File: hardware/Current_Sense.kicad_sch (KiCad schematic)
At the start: 0 parts

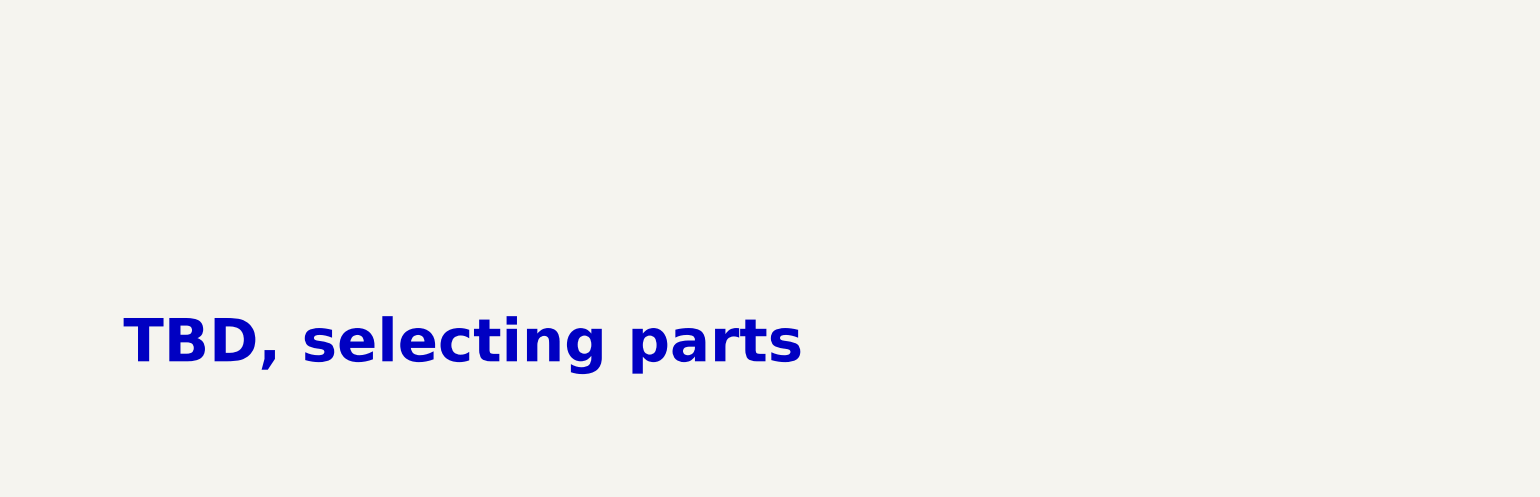
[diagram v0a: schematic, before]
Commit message: added designs for LZSR-80P and AMC class voltage sense
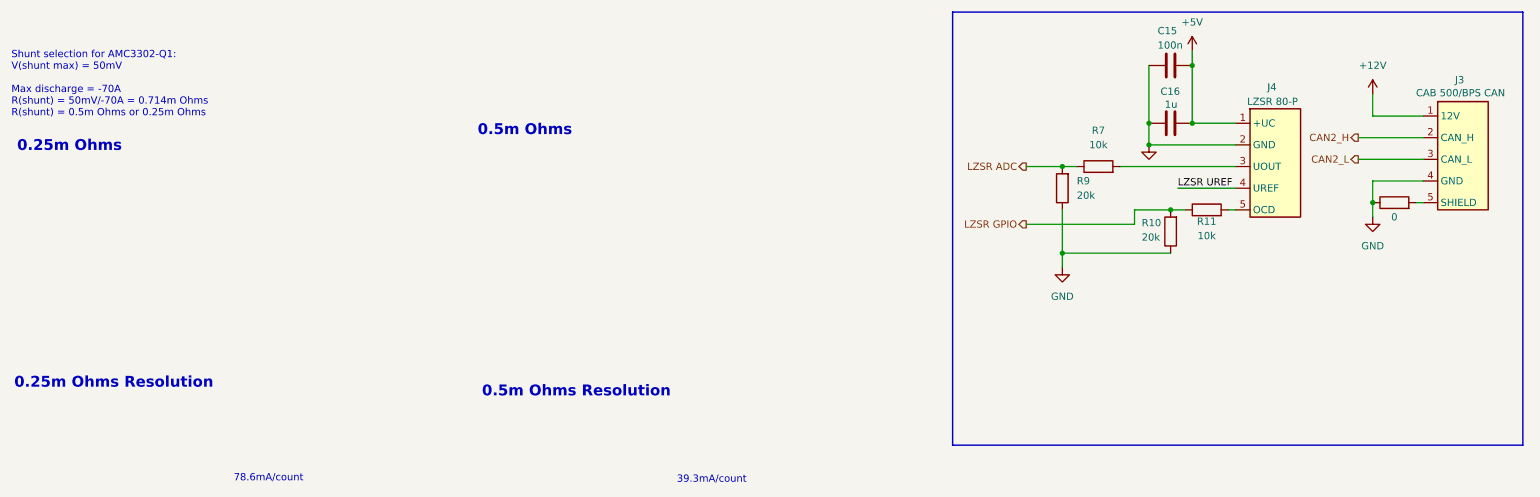
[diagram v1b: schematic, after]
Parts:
- added C15: 100n, symbol Device:C
- added C16: 1u, symbol Device:C
- added J3: CAB 500/BPS CAN, LHRS_Connectors:Molex_Nano-Fit_105309-xx05_1x05_P2.50mm_Vertical, symbol lhrs_connectors:CAN_NANO_01x05
- added J4: LZSR 80-P, LHRS_Connectors:Molex_Nano-Fit_105309-xx05_1x05_P2.50mm_Vertical, symbol lhrs_connectors:CAN_NANO_01x05
- added R10, R9: 20k, symbol Device:R
- added R11, R7: 10k, symbol Device:R
- added R6: 0, symbol Device:R
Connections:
- new net: J3.5 (SHIELD), R6.2
- new net: J4.3 (UOUT), R7.2
- new net: J4.5 (OCD), R11.2
- new net +12V: J3.1 (12V)
- new net +5V: C15.1, C16.1, J4.1 (+UC)
- new net CAN2_H: J3.2 (CAN_H)
- new net CAN2_L: J3.3 (CAN_L)
- new net GND: C15.2, C16.2, J3.4 (GND), J4.2 (GND), R10.1, R6.1, R9.1
- new net LZSR ADC: R7.1, R9.2
- new net LZSR GPIO: R10.2, R11.1
- new net LZSR UREF: J4.4 (UREF)
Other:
- note added: "0.25m Ohms"
- note added: "0.25m Ohms Resolution"
- note added: "0.5m Ohms"
- note added: "0.5m Ohms Resolution"
- note added: "39.3mA/count"
- note added: "78.6mA/count"
- note added: "Shunt selection for AMC3302-Q1: V(shunt max) = 50mV Max discharge = -70A R(shunt) = 50mV/-70A = 0.714m Ohms R(shunt) = 0.5m Ohms or 0.25m Ohms"
- note removed: "TBD, selecting parts"

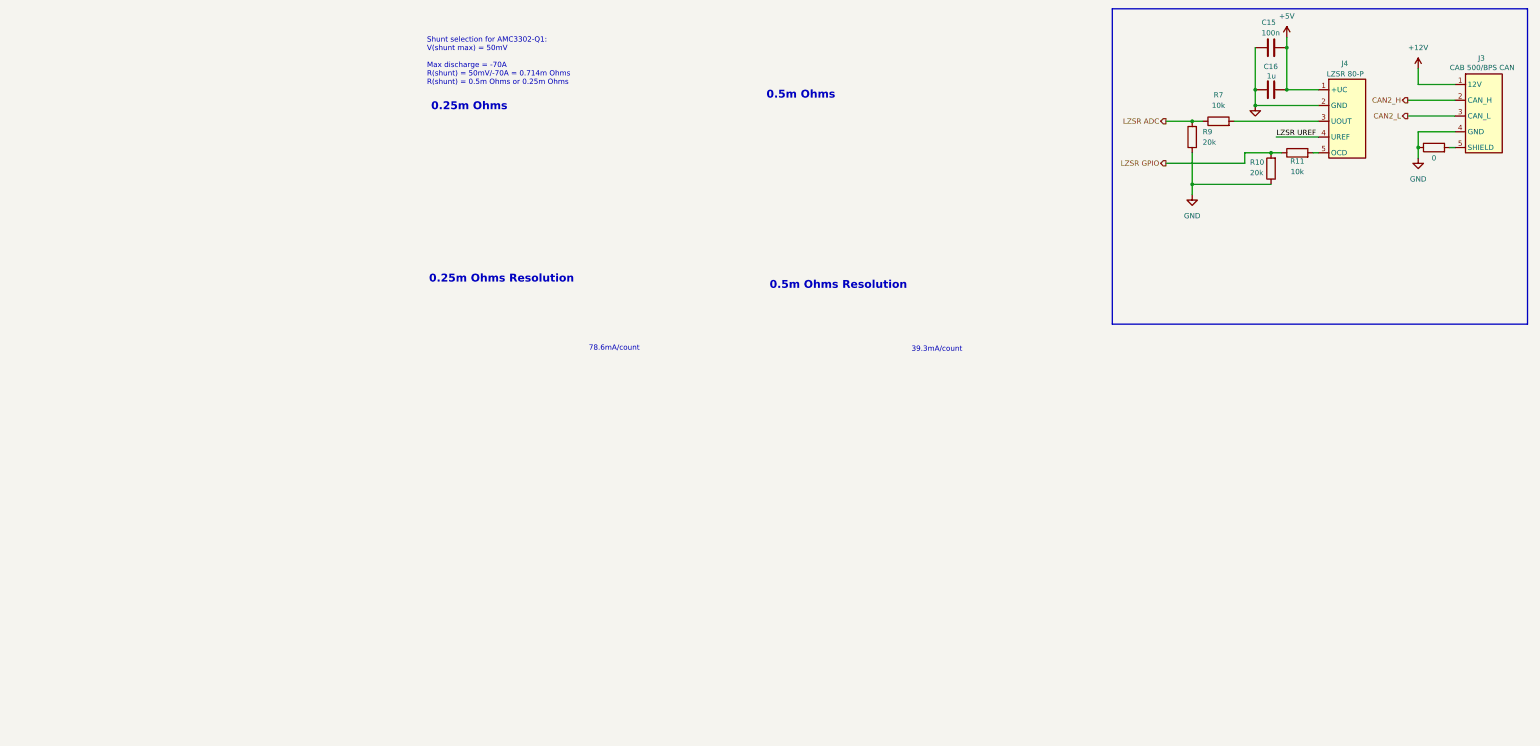
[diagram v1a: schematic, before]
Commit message: labeled + stm32 cube layout
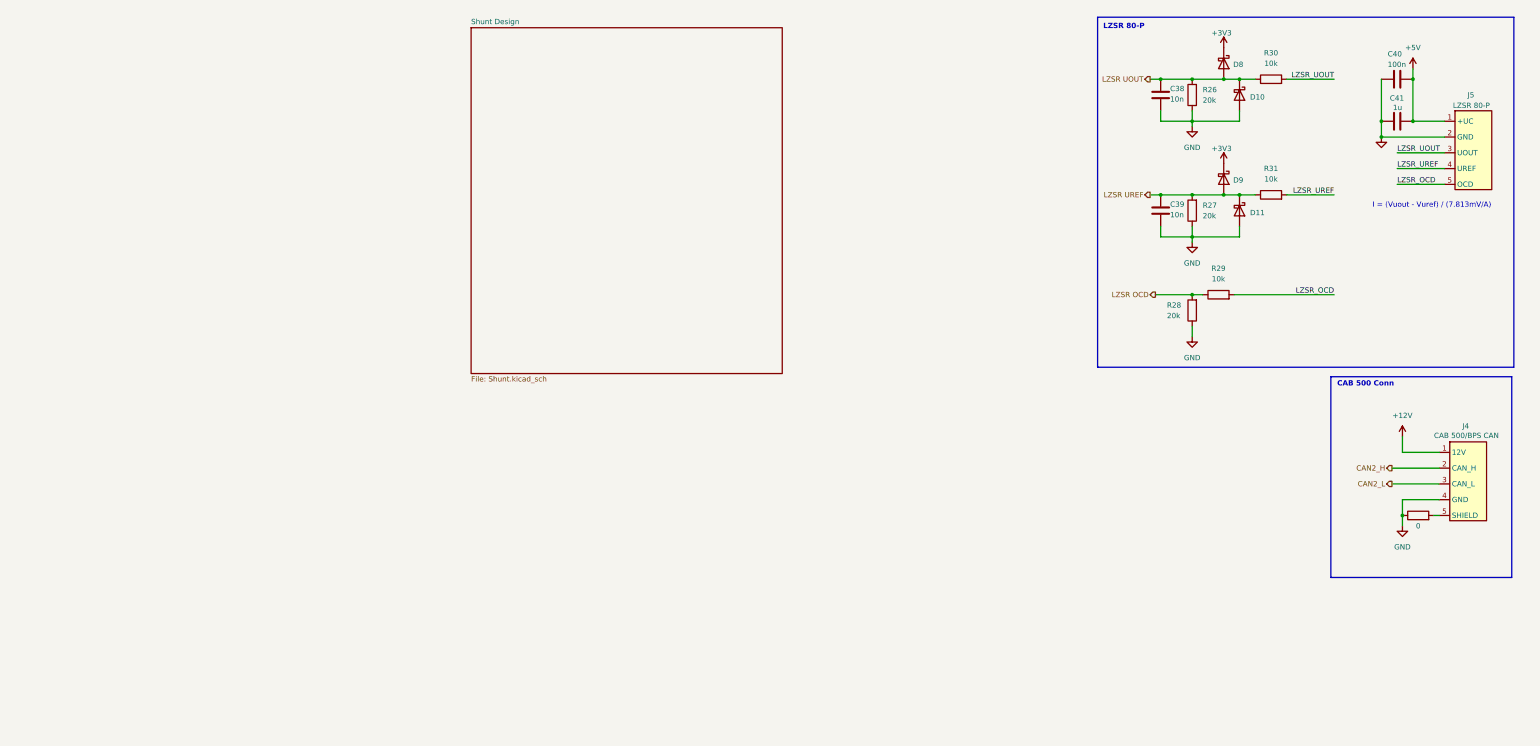
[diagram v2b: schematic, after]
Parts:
- added C38, C39: 10n, symbol Device:C
- added D10, D11, D8, D9: ~, symbol Device:D_Schottky
- added R27: 20k, symbol Device:R
- added R31: 10k, symbol Device:R
- renumbered C15 to C40, C16 to C41, J3 to J4, J4 to J5, R9 to R26, R10 to R28, R11 to R29, R7 to R30, R6 to R32
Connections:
- net GND: now also C38.2, C39.2, D10.2 (A), D11.2 (A), R27.1
- net LZSR UREF: now also C39.1, D11.1 (K), D9.2 (A), R27.2, R31.1; no longer J5.4 (UREF)
- net LZSR_UOUT: now reaches J5.3 (UOUT), R30.2
- net LZSR_OCD: now reaches J5.5 (OCD), R29.2
- net LZSR ADC renamed LZSR UOUT
- net LZSR UOUT: now also C38.1, D10.1 (K), D8.2 (A)
- net LZSR GPIO renamed LZSR OCD
- new net +3V3: D8.1 (K), D9.1 (K)
- new net LZSR_UREF: J5.4 (UREF), R31.2
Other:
- added sheet Shunt Design (Shunt.kicad_sch)
- note added: "CAB 500 Conn"
- note added: "I = (Vuout - Vuref) / (7.813mV/A)"
- note added: "LZSR 80-P"
- note removed: "0.25m Ohms"
- note removed: "0.25m Ohms Resolution"
- note removed: "0.5m Ohms"
- note removed: "0.5m Ohms Resolution"
- note removed: "39.3mA/count"
- note removed: "78.6mA/count"
- note removed: "Shunt selection for AMC3302-Q1: V(shunt max) = 50mV Max discharge = -70A R(shunt) = 50mV/-70A = 0.714m Ohms R(shunt) = 0.5m Ohms or 0.25m Ohms"
- moved on the sheet: C40, C41, J4, J5, R26, R28, R29, R30

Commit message: added debug led
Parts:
- renumbered D8 to D15, D9 to D16, D10 to D17, D11 to D18, R26 to R33, R27 to R34, R28 to R35, R29 to R36, R30 to R37, R31 to R38, R32 to R39
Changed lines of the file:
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@@
 		(dnp no)
 		(fields_autoplaced yes)
-		(property "Reference" "R31"
+		(property "Reference" "R38"
 			(at 222.25 53.34 90)
 			(effects
@@
 			(project "PS-HVCarrier"
 				(path "/2365a867-6254-4a7c-9718-f325e0bbac5c/c64f1e33-0c51-411c-bbbf-0af7b620c655"
-					(reference "R31")
+					(reference "R38")
 					(unit 1)
 				)
@@
 		(dnp no)
 		(fields_autoplaced yes)
-		(property "Reference" "R27"
+		(property "Reference" "R34"
 			(at 205.74 62.2299 0)
 			(effects
@@
 			(project "PS-HVCarrier"
 				(path "/2365a867-6254-4a7c-9718-f325e0bbac5c/c64f1e33-0c51-411c-bbbf-0af7b620c655"
-					(reference "R27")
+					(reference "R34")
 					(unit 1)
 				)
@@
 		(dnp no)
 		(fields_autoplaced yes)
-		(property "Reference" "#PWR043"
+		(property "Reference" "#PWR051"
 			(at 203.2 49.53 0)
 			(effects
@@
 			(project "PS-HVCarrier"
 				(path "/2365a867-6254-4a7c-9718-f325e0bbac5c/c64f1e33-0c51-411c-bbbf-0af7b620c655"
-					(reference "#PWR043")
+					(reference "#PWR051")
 					(unit 1)
 				)
@@
 		(dnp no)
 		(fields_autoplaced yes)
-		(property "Reference" "#PWR051"
+		(property "Reference" "#PWR059"
 			(at 256.54 33.02 0)
 			(effects
@@
 			(project "PS-HVCarrier"
 				(path "/2365a867-6254-4a7c-9718-f325e0bbac5c/c64f1e33-0c51-411c-bbbf-0af7b620c655"
-					(reference "#PWR051")
+					(reference "#PWR059")
 					(unit 1)
 				)
@@
 		(dnp no)
 		(fields_autoplaced yes)
-		(property "Reference" "#PWR044"
+		(property "Reference" "#PWR052"
 			(at 203.2 77.47 0)
 			(effects
@@
 			(project "PS-HVCarrier"
 				(path "/2365a867-6254-4a7c-9718-f325e0bbac5c/c64f1e33-0c51-411c-bbbf-0af7b620c655"
-					(reference "#PWR044")
+					(reference "#PWR052")
 					(unit 1)
 				)
@@
 		(on_board yes)
 		(dnp no)
-		(property "Reference" "#PWR046"
+		(property "Reference" "#PWR054"
 			(at 210.82 27.94 0)
 			(effects
@@
 			(project ""
 				(path "/2365a867-6254-4a7c-9718-f325e0bbac5c/c64f1e33-0c51-411c-bbbf-0af7b620c655"
-					(reference "#PWR046")
+					(reference "#PWR054")
 					(unit 1)
 				)
@@
 		(dnp no)
 		(fields_autoplaced yes)
-		(property "Reference" "R26"
+		(property "Reference" "R33"
 			(at 205.74 34.2899 0)
 			(effects
@@
 			(project "PS-HVCarrier"
 				(path "/2365a867-6254-4a7c-9718-f325e0bbac5c/c64f1e33-0c51-411c-bbbf-0af7b620c655"
-					(reference "R26")
+					(reference "R33")
 					(unit 1)
 				)
@@
 		(on_board yes)
 		(dnp no)
-		(property "Reference" "R28"
+		(property "Reference" "R35"
 			(at 197.104 86.36 0)
 			(effects
@@
 			(project "PS-HVCarrier"
 				(path "/2365a867-6254-4a7c-9718-f325e0bbac5c/c64f1e33-0c51-411c-bbbf-0af7b620c655"
-					(reference "R28")
+					(reference "R35")
 					(unit 1)
 				)
@@
 		(on_board yes)
 		(dnp no)
-		(property "Reference" "D11"
+		(property "Reference" "D18"
 			(at 217.17 64.008 90)
 			(effects
@@
 			(project "PS-HVCarrier"
 				(path "/2365a867-6254-4a7c-9718-f325e0bbac5c/c64f1e33-0c51-411c-bbbf-0af7b620c655"
-					(reference "D11")
+					(reference "D18")
 					(unit 1)
 				)
@@
 		(dnp no)
 		(fields_autoplaced yes)
-		(property "Reference" "#PWR048"
+		(property "Reference" "#PWR056"
 			(at 248.92 52.07 0)
 			(effects
@@
 			(project "PS-HVCarrier"
 				(path "/2365a867-6254-4a7c-9718-f325e0bbac5c/c64f1e33-0c51-411c-bbbf-0af7b620c655"
-					(reference "#PWR048")
+					(reference "#PWR056")
 					(unit 1)
 				)
@@
 		(on_board yes)
 		(dnp no)
-		(property "Reference" "D10"
+		(property "Reference" "D17"
 			(at 217.17 36.068 90)
 			(effects
@@
 			(project "PS-HVCarrier"
 				(path "/2365a867-6254-4a7c-9718-f325e0bbac5c/c64f1e33-0c51-411c-bbbf-0af7b620c655"
-					(reference "D10")
+					(reference "D17")
 					(unit 1)
 				)
@@
 		(on_board yes)
 		(dnp no)
-		(property "Reference" "D9"
+		(property "Reference" "D16"
 			(at 213.106 56.134 90)
 			(effects
@@
 			(project "PS-HVCarrier"
 				(path "/2365a867-6254-4a7c-9718-f325e0bbac5c/c64f1e33-0c51-411c-bbbf-0af7b620c655"
-					(reference "D9")
+					(reference "D16")
 					(unit 1)
 				)
@@
 		(dnp no)
 		(fields_autoplaced yes)
-		(property "Reference" "#PWR050"
+		(property "Reference" "#PWR058"
 			(at 254 146.05 0)
 			(effects
@@
 			(project "PS-HVCarrier"
 				(path "/2365a867-6254-4a7c-9718-f325e0bbac5c/c64f1e33-0c51-411c-bbbf-0af7b620c655"
-					(reference "#PWR050")
+					(reference "#PWR058")
 					(unit 1)
 				)
@@
 		(on_board yes)
 		(dnp no)
-		(property "Reference" "#PWR047"
+		(property "Reference" "#PWR055"
 			(at 210.82 55.88 0)
 			(effects
@@
 			(project "PS-HVCarrier"
 				(path "/2365a867-6254-4a7c-9718-f325e0bbac5c/c64f1e33-0c51-411c-bbbf-0af7b620c655"
-					(reference "#PWR047")
+					(reference "#PWR055")
 					(unit 1)
 				)
@@
 		(dnp no)
 		(fields_autoplaced yes)
-		(property "Reference" "#PWR045"
+		(property "Reference" "#PWR053"
 			(at 203.2 100.33 0)
 			(effects
@@
 			(project ""
 				(path "/2365a867-6254-4a7c-9718-f325e0bbac5c/c64f1e33-0c51-411c-bbbf-0af7b620c655"
-					(reference "#PWR045")
+					(reference "#PWR053")
 					(unit 1)
 				)
@@
 		(on_board yes)
 		(dnp no)
-		(property "Reference" "D8"
+		(property "Reference" "D15"
 			(at 213.106 28.194 90)
 			(effects
@@
 			(project ""
 				(path "/2365a867-6254-4a7c-9718-f325e0bbac5c/c64f1e33-0c51-411c-bbbf-0af7b620c655"
-					(reference "D8")
+					(reference "D15")
 					(unit 1)
 				)
@@
 		(on_board yes)
 		(dnp no)
-		(property "Reference" "R29"
+		(property "Reference" "R36"
 			(at 209.55 77.47 90)
 			(effects
@@
 			(project "PS-HVCarrier"
 				(path "/2365a867-6254-4a7c-9718-f325e0bbac5c/c64f1e33-0c51-411c-bbbf-0af7b620c655"
-					(reference "R29")
+					(reference "R36")
 					(unit 1)
 				)
@@
 		(dnp no)
 		(fields_autoplaced yes)
-		(property "Reference" "#PWR049"
+		(property "Reference" "#PWR057"
 			(at 254 121.92 0)
 			(effects
@@
 			(project "PS-HVCarrier"
 				(path "/2365a867-6254-4a7c-9718-f325e0bbac5c/c64f1e33-0c51-411c-bbbf-0af7b620c655"
-					(reference "#PWR049")
+					(reference "#PWR057")
 					(unit 1)
 				)
@@
 		(on_board yes)
 		(dnp no)
-		(property "Reference" "R32"
+		(property "Reference" "R39"
 			(at 257.81 130.81 90)
 			(effects
@@
 			(project "PS-HVCarrier"
 				(path "/2365a867-6254-4a7c-9718-f325e0bbac5c/c64f1e33-0c51-411c-bbbf-0af7b620c655"
-					(reference "R32")
+					(reference "R39")
 					(unit 1)
 				)
@@
 		(dnp no)
 		(fields_autoplaced yes)
-		(property "Reference" "R30"
+		(property "Reference" "R37"
 			(at 222.25 25.4 90)
 			(effects
@@
 			(project "PS-HVCarrier"
 				(path "/2365a867-6254-4a7c-9718-f325e0bbac5c/c64f1e33-0c51-411c-bbbf-0af7b620c655"
-					(reference "R30")
-					(unit 1)
-				)
+					(reference "R37")
+					(unit 1)
+				)

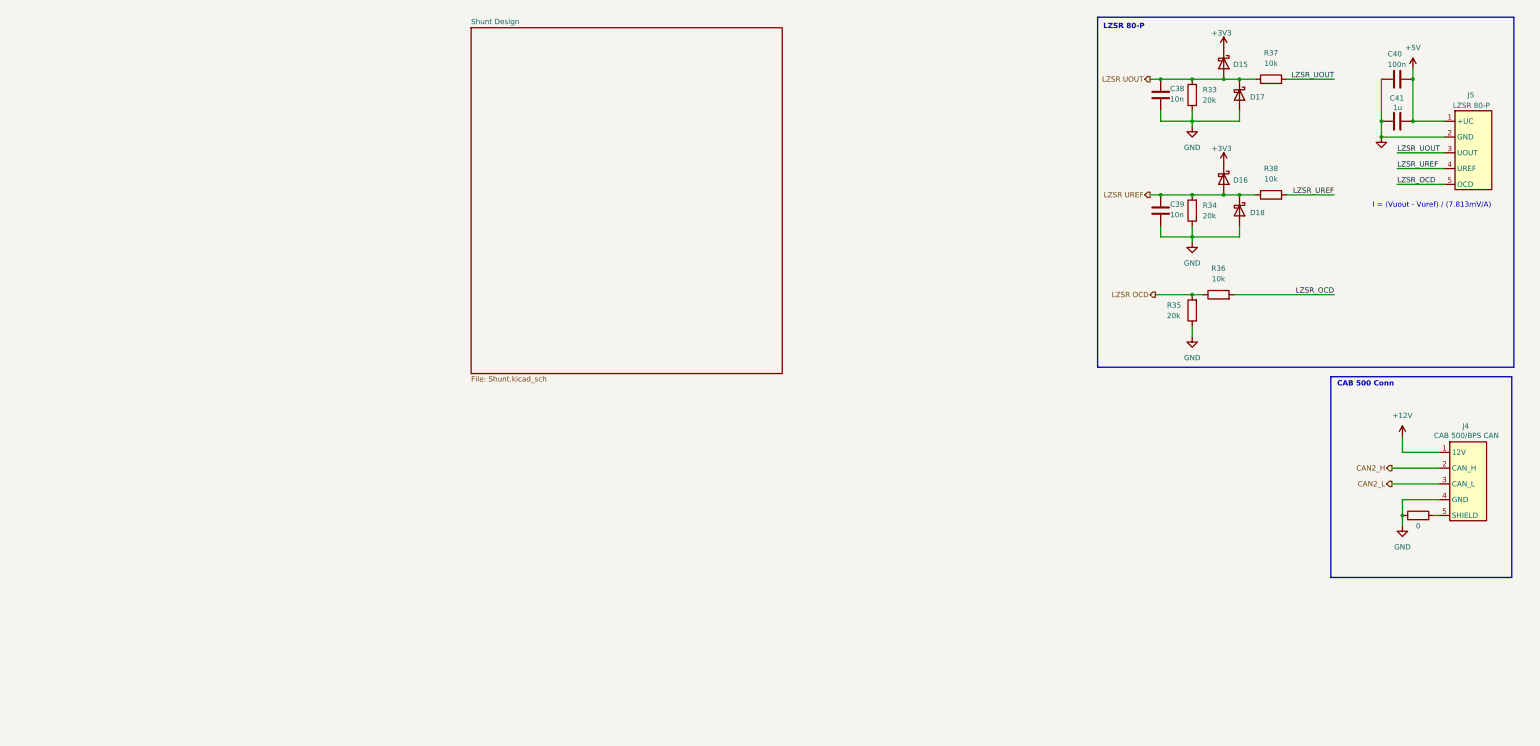
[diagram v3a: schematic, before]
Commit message: addressed 75% of review council 2, cleaned up ERC errors, embedded datasheet and PN
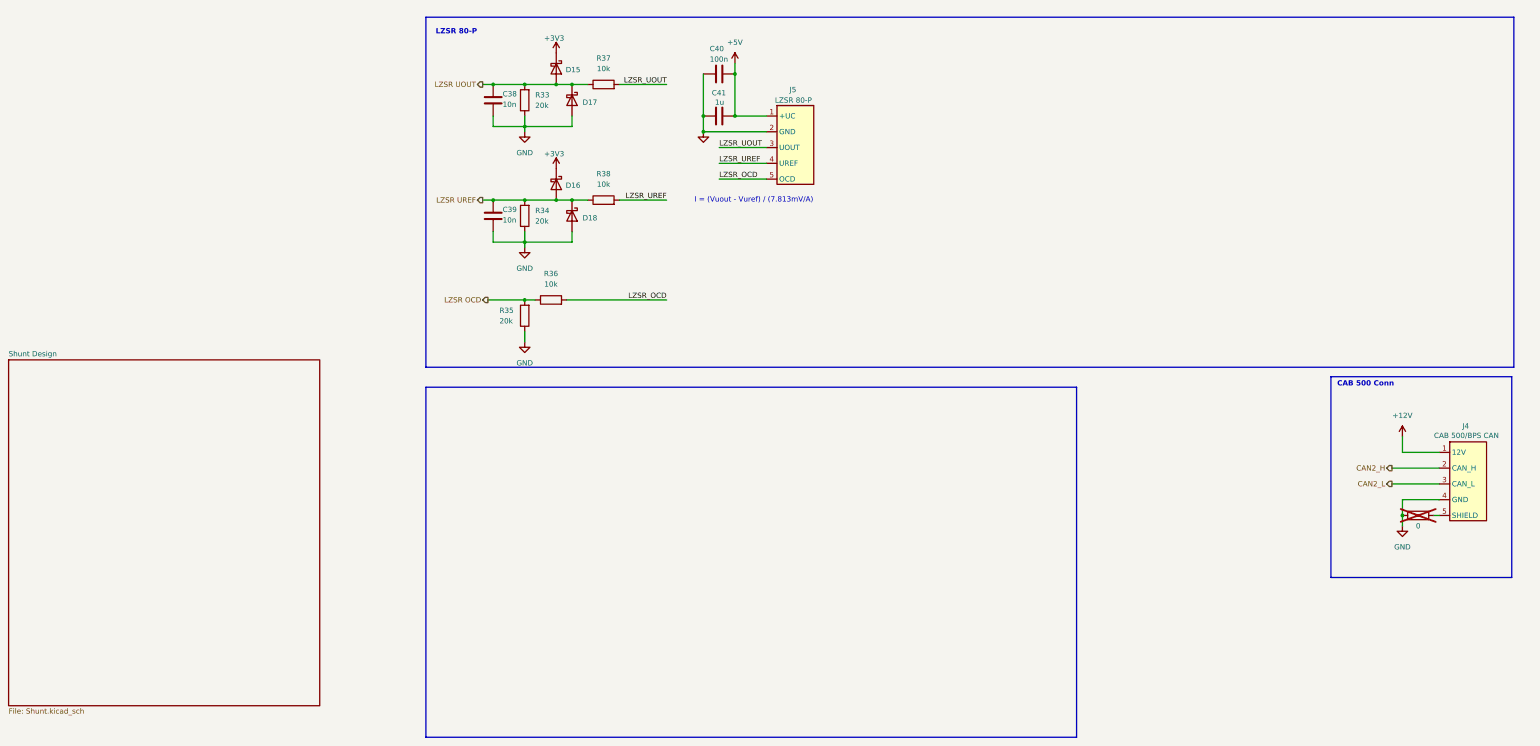
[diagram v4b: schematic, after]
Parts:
- D15, D16, D17, D18: value ~ -> (none)
- R39: now not fitted
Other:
- moved on the sheet: C38, C39, C40, C41, D15, D16, D17, D18, J5, R33, R34, R35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
